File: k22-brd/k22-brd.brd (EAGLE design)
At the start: 22.9 x 63.5 mm, 34 parts, among them J1 61302011121, J2 61302011121, J3 CORTEX_DEBUG_PTH

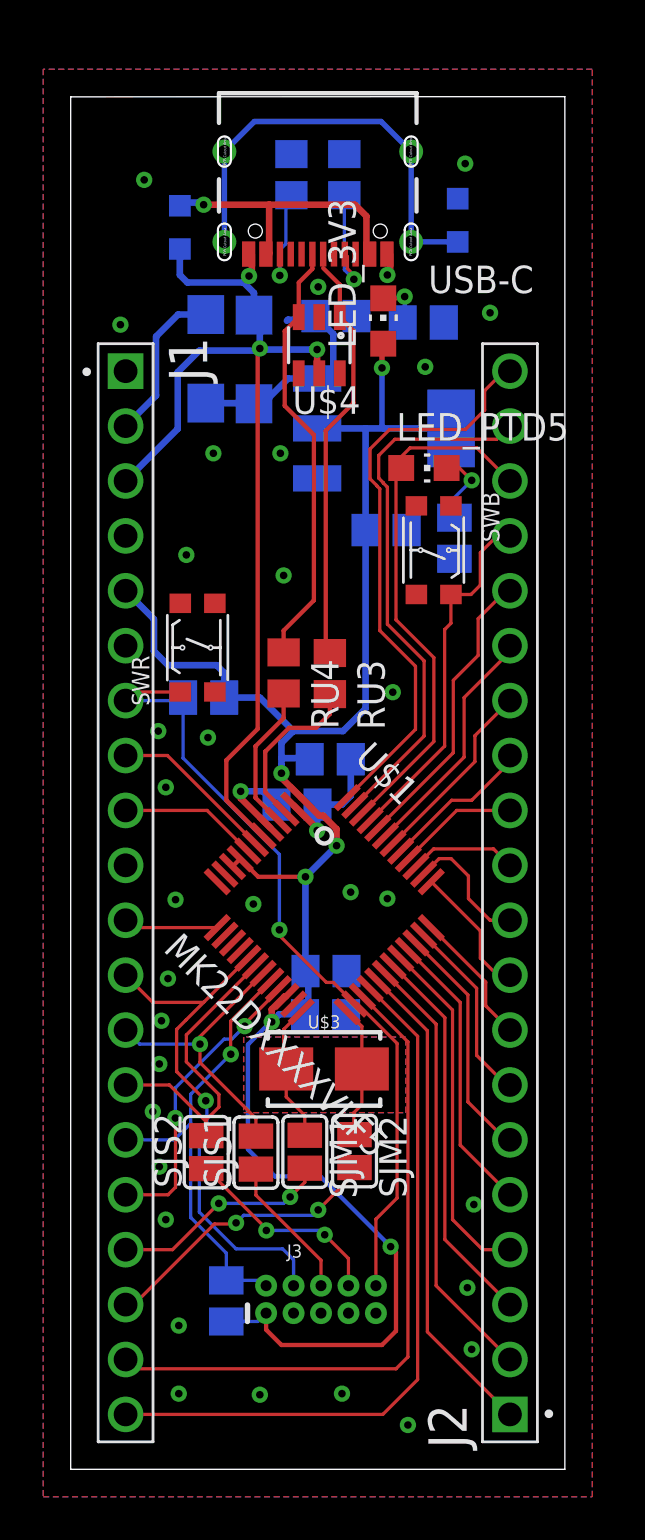
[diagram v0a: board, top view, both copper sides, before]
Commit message: Different pin order on headers
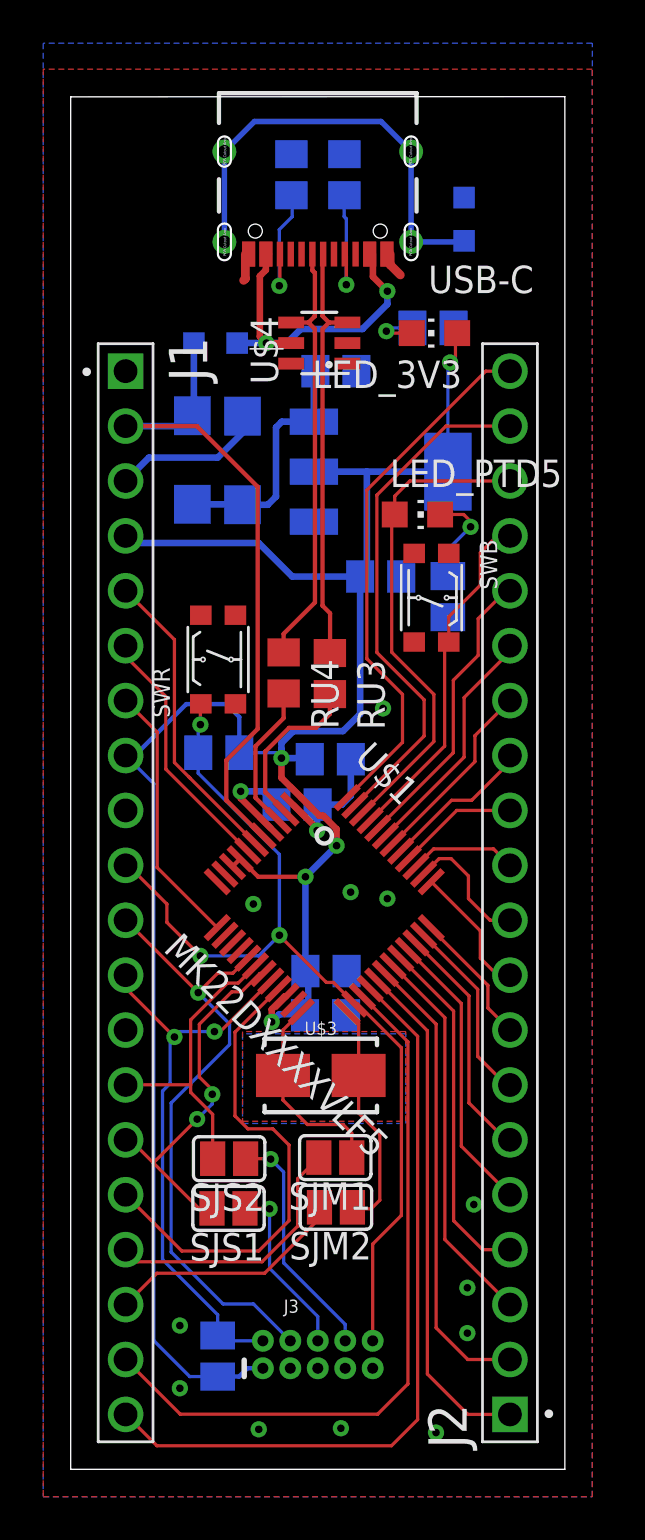
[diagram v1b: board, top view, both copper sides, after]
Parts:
- moved LU1 5.60 mm to (6.70, 52.1), turned to 180 degrees
- moved DV1 5.45 mm to (5.63, 46.7)
- moved DV2 5.00 mm to (7.95, 46.7)
- moved SJS1 2.88 mm to (7.30, 12.1), turned to 180 degrees
- moved SJM2 2.74 mm to (12.3, 12.1), turned to 180 degrees
- moved RL1 2.72 mm to (17.4, 40.4)
- moved RR1 2.64 mm to (6.85, 33.1)
- moved RS2 2.58 mm to (6.80, 5.24)
- moved J3 2.55 mm to (11.4, 5.31)
- moved CV1 2.55 mm to (12.3, 50.8)
- moved LED_3V3 2.44 mm to (16.8, 52.6), turned to 90 degrees
- moved SWB 2.20 mm to (16.7, 40.3)
- moved LED_PTD5 2.17 mm to (16.0, 44.2)
- moved CV2 2.16 mm to (14.3, 41.3)
- moved U$2 2.01 mm to (14.3, 46.1)
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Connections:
- removed net N$5: J1.4
- net 3V3: now also J1.4, J1.8; no longer J1.5
- net D+CON: now also U$4.3; no longer U$4.1
- net D-CON: now also U$4.4; no longer U$4.3
- net DM0: now also J1.6; no longer J1.9
- net DP0: now also J1.5; no longer J1.8
- net GND: now also J1.13, J1.9; no longer J1.10, J1.6
- net RESET: now also J1.10; no longer J1.7
- net SWD_CLK: now also J1.11; no longer J1.12
- net SWD_DIO: now also J1.12; no longer J1.15
- net UART_TX: now also J1.15; no longer J1.13
- net USB5V: now also J1.2; no longer J1.3, U$4.5
- net VBUSCON: now also U$4.5
- net VIN: now also J1.3; no longer J1.2
- net VREF: now also J1.7; no longer J1.11
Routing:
- net 3V3: track 91.7 -> 107.0 mm, vias 6 -> 5
- net USB5V: track 45.7 -> 31.7 mm, vias 2 -> 0
- net PTA4: track 13.8 -> 22.6 mm, vias 2 -> 0
- net VREF: track 4.38 -> 12.3 mm
- net RESET: track 37.4 -> 44.1 mm, vias 1 -> 3
- net DP0: track 7.69 -> 14.2 mm
- net DM0: track 6.44 -> 11.8 mm
- net SWD_DIO: track 21.3 -> 26.7 mm, vias 1 -> 2
- net PTA19_OSC: track 6.14 -> 10.8 mm
- net SWD_CLK: track 24.4 -> 28.6 mm
- net UART_TX: track 13.5 -> 17.0 mm, vias 1 -> 2
- net VBUSCON: track 13.1 -> 16.2 mm, vias 1 -> 2
- net PTA18_OSC: track 6.46 -> 9.39 mm
- net PTB0: track 31.0 -> 33.5 mm
- net PTB1: track 33.2 -> 35.5 mm
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
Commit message: Fixed DRC errors
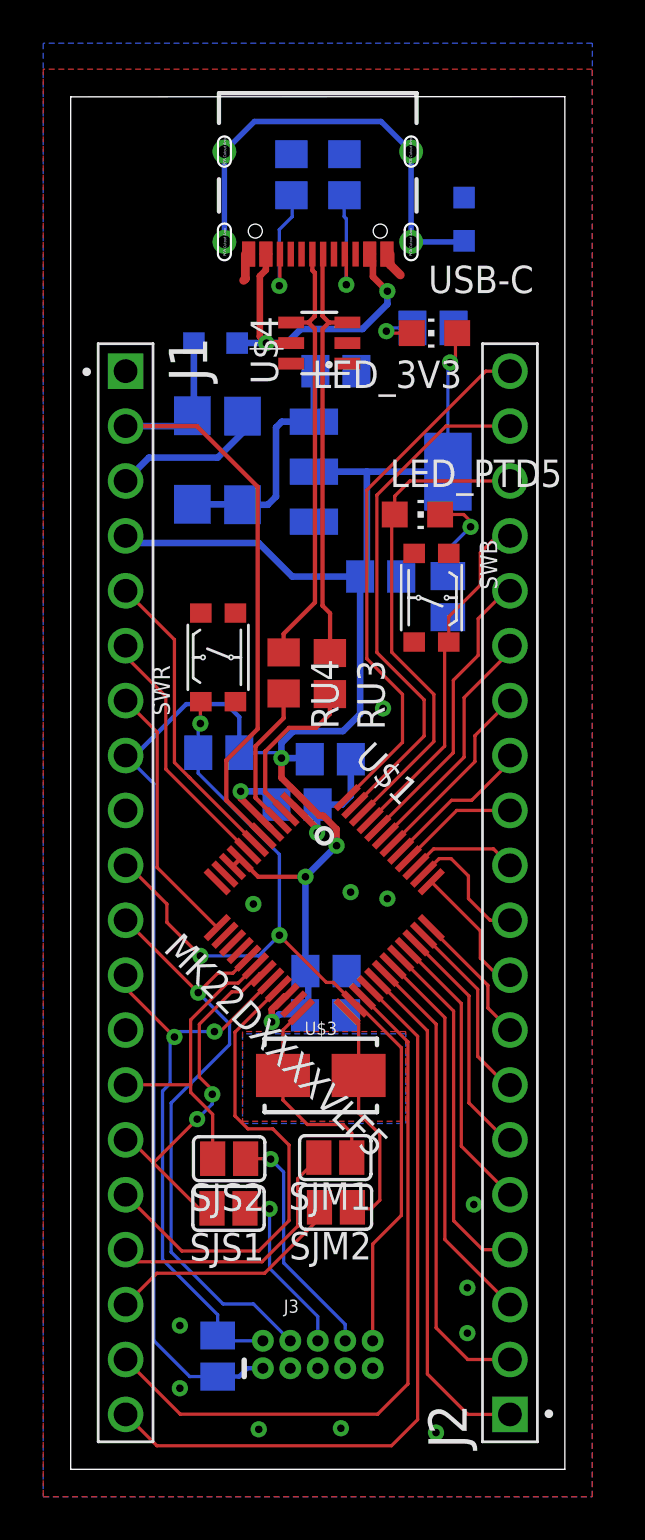
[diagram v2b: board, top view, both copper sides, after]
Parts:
- moved SWR 0.10 mm to (6.82, 37.6)
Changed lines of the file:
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@@
 <attribute name="VALUE" x="13.94" y="43.09" size="0.8128" layer="27" rot="R270"/>
 </element>
-<element name="SWR" library="Switch" library_urn="urn:adsk.eagle:library:11396471" package="KMR731NGLFS" package3d_urn="urn:adsk.eagle:package:17224188/5" value="KMR731NGLFS" x="6.82" y="37.46" smashed="yes" rot="R90">
-<attribute name="CREATED_BY" value="PCBLayout.com" x="50" y="84.45" size="1.778" layer="27" rot="R90" display="off"/>
-<attribute name="DIGIKEY_PARTNO" value="CKN10687CT-ND" x="50" y="84.45" size="1.778" layer="27" rot="R90" display="off"/>
-<attribute name="MANUFACTURER" value="C&amp;K" x="50" y="84.45" size="1.778" layer="27" rot="R90" display="off"/>
-<attribute name="MPN" value="KMR731NG LFS" x="50" y="84.45" size="1.778" layer="27" rot="R90" display="off"/>
-<attribute name="NAME" x="4.59" y="34.77" size="0.8128" layer="25" rot="R90"/>
-<attribute name="VALUE" x="9.57" y="34.69" size="0.8128" layer="27" rot="R90"/>
+<element name="SWR" library="Switch" library_urn="urn:adsk.eagle:library:11396471" package="KMR731NGLFS" package3d_urn="urn:adsk.eagle:package:17224188/5" value="KMR731NGLFS" x="6.82" y="37.56" smashed="yes" rot="R90">
+<attribute name="CREATED_BY" value="PCBLayout.com" x="50" y="84.55" size="1.778" layer="27" rot="R90" display="off"/>
+<attribute name="DIGIKEY_PARTNO" value="CKN10687CT-ND" x="50" y="84.55" size="1.778" layer="27" rot="R90" display="off"/>
+<attribute name="MANUFACTURER" value="C&amp;K" x="50" y="84.55" size="1.778" layer="27" rot="R90" display="off"/>
+<attribute name="MPN" value="KMR731NG LFS" x="50" y="84.55" size="1.778" layer="27" rot="R90" display="off"/>
+<attribute name="NAME" x="4.59" y="34.87" size="0.8128" layer="25" rot="R90"/>
+<attribute name="VALUE" x="9.57" y="34.79" size="0.8128" layer="27" rot="R90"/>
 </element>
 <element name="U$1" library="poli-MK22" package="TQFP48_7X7" value="MK22DXXXXVLF5" x="11.73" y="26.12" smashed="yes" rot="R315">
@@
 <contactref element="U$2" pad="1"/>
 <wire x1="10.315784375" y1="30.71619375" x2="11.4" y2="29.631978125" width="0.3048" layer="1"/>
-<wire x1="11.4" y1="29.631978125" x2="11.4" y2="29.55" width="0.3048" layer="1"/>
-<via x="11.4" y="29.55" extent="1-16" drill="0.35"/>
-<wire x1="11.4" y1="29.55" x2="11.4" y2="30.73" width="0.3048" layer="16"/>
+<wire x1="11.4" y1="29.631978125" x2="11.4" y2="29.45" width="0.3048" layer="1"/>
+<via x="11.4" y="29.45" extent="1-16" drill="0.35"/>
+<wire x1="11.4" y1="29.45" x2="11.4" y2="30.73" width="0.3048" layer="16"/>
 <wire x1="11.4" y1="30.73" x2="11.42" y2="30.75" width="0.3048" layer="16"/>
 <wire x1="11.42" y1="30.75" x2="12.55" y2="30.75" width="0.3048" layer="16"/>
@@
 <wire x1="9.05" y1="52.1" x2="7.7" y2="52.1" width="0.3048" layer="16"/>
 <wire x1="9.05" y1="52.1" x2="10.2" y2="52.1" width="0.3048" layer="1"/>
-<wire x1="13.68" y1="56.215" x2="13.93" y2="55.965" width="0.3048" layer="1"/>
 <wire x1="13.5" y1="52.75" x2="10.65" y2="52.75" width="0.3048" layer="16"/>
 <wire x1="10.65" y1="52.75" x2="10" y2="52.1" width="0.3048" layer="16"/>
@@
 <wire x1="8.75" y1="55.2" x2="8.75" y2="52.4" width="0.3048" layer="1"/>
 <wire x1="8.75" y1="52.4" x2="9.05" y2="52.1" width="0.3048" layer="1"/>
-<wire x1="13.98" y1="56.215" x2="13.98" y2="55.17" width="0.3048" layer="1"/>
 <wire x1="13.98" y1="55.17" x2="14.65" y2="54.5" width="0.3048" layer="1"/>
 <via x="14.65" y="54.5" extent="1-16" drill="0.35"/>
 <wire x1="14.65" y1="54.5" x2="14.65" y2="53.9" width="0.3048" layer="16"/>
 <wire x1="14.65" y1="53.9" x2="13.5" y2="52.75" width="0.3048" layer="16"/>
-<wire x1="13.98" y1="56.215" x2="13.93" y2="55.965" width="0" layer="19" extent="1-1"/>
-<wire x1="8.88" y1="56.215" x2="9.18" y2="56.215" width="0" layer="19" extent="1-1"/>
+<wire x1="13.68" y1="56.215" x2="13.98" y2="55.915" width="0.3048" layer="1"/>
+<wire x1="13.98" y1="55.915" x2="13.98" y2="55.17" width="0.3048" layer="1"/>
+<wire x1="13.98" y1="56.215" x2="13.68" y2="56.215" width="0.3048" layer="1"/>
+<wire x1="9.18" y1="56.215" x2="8.88" y2="56.215" width="0.3048" layer="1"/>
 </signal>
 <signal name="CC1CON">
@@
 <contactref element="U$4" pad="4"/>
 <wire x1="11.3" y1="40.1" x2="9.85" y2="38.65" width="0.2" layer="1"/>
-<wire x1="11.3" y1="52.6" x2="11.3" y2="40.1" width="0.2" layer="1"/>
 <wire x1="11.2968" y1="55.3482" x2="11.18" y2="55.465" width="0.2032" layer="1"/>
 <wire x1="11.18" y1="56.215" x2="11.18" y2="55.465" width="0.2032" layer="1"/>
@@
 <wire x1="11.2968" y1="53.3468" x2="11" y2="53.05" width="0.2032" layer="1"/>
 <wire x1="11" y1="53.05" x2="10.2" y2="53.05" width="0.2032" layer="1"/>
-<wire x1="11.2968" y1="52.7532" x2="11.2968" y2="52.60369375" width="0.2032" layer="1"/>
-<wire x1="11.2968" y1="52.60369375" x2="11.2984" y2="52.60209375" width="0.2032" layer="1"/>
-<wire x1="11.2984" y1="52.60209375" x2="11.2984" y2="52.6" width="0.2032" layer="1"/>
 <wire x1="11" y1="53.05" x2="11.2968" y2="52.7532" width="0.2032" layer="1"/>
+<wire x1="11.2968" y1="52.7532" x2="11.2984" y2="52.7516" width="0.2" layer="1"/>
+<wire x1="11.2984" y1="52.7516" x2="11.2984" y2="52.6043625" width="0.2" layer="1"/>
+<wire x1="11.2984" y1="52.6043625" x2="11.3" y2="52.6027625" width="0.2" layer="1"/>
+<wire x1="11.3" y1="52.6027625" x2="11.3" y2="40.1" width="0.2" layer="1"/>
 <wire x1="11.18" y1="56.215" x2="12.18" y2="56.215" width="0" layer="19" extent="1-1"/>
-<wire x1="11.3" y1="52.6" x2="11.2984" y2="52.6" width="0" layer="19" extent="1-1"/>
 </signal>
 <signal name="CC2CON">
@@
 <wire x1="5.63" y1="48.53" x2="5.63" y2="48.74" width="0.3048" layer="16"/>
 <wire x1="5.36" y1="48.26" x2="5.63" y2="48.53" width="0.3048" layer="16"/>
-<wire x1="5.55" y1="48.82" x2="5.63" y2="48.74" width="0.3048" layer="16"/>
 <wire x1="8.65" y1="34.25" x2="8.65" y2="45.45" width="0.2032" layer="1"/>
 <wire x1="5.84" y1="48.26" x2="2.54" y2="48.26" width="0.2032" layer="1"/>
@@
 <contactref element="RU3" pad="2"/>
 <contactref element="U$1" pad="3"/>
-<wire x1="11.99" y1="35.86" x2="11.89" y2="35.76" width="0.2" layer="1"/>
 <wire x1="10.1" y1="34.3" x2="9" y2="33.2" width="0.2" layer="1"/>
 <wire x1="9" y1="31.324871875" x2="9.96223125" y2="30.362640625" width="0.2" layer="1"/>
@@
 <contactref element="J3" pad="2"/>
 <contactref element="RS2" pad="2"/>
-<wire x1="6.8" y1="6.19" x2="6.75" y2="6.24" width="0.1524" layer="16"/>
 <wire x1="8.89" y1="5.945" x2="7.045" y2="5.945" width="0.1524" layer="16"/>
 <wire x1="7.045" y1="5.945" x2="6.8" y2="6.19" width="0.1524" layer="16"/>
@@
 <contactref element="U$1" pad="21"/>
 <contactref element="J1" pad="16"/>
-<wire x1="9.608678125" y1="22.2309125" x2="9.608678125" y2="22.158678125" width="0.1524" layer="1"/>
 <wire x1="9.608678125" y1="22.2309125" x2="7.6" y2="20.222234375" width="0.1524" layer="1"/>
 <wire x1="7.6" y1="20.222234375" x2="7.6" y2="16.35" width="0.1524" layer="1"/>
@@
 <wire x1="9.655190625" y1="24.694809375" x2="11.826196875" y2="22.523803125" width="0.1524" layer="1"/>
 <contactref element="J1" pad="10"/>
-<wire x1="5.9" y1="33.15" x2="5.9" y2="34.35" width="0.1524" layer="16"/>
-<wire x1="5.9" y1="34.35" x2="6" y2="34.45" width="0.1524" layer="16"/>
-<via x="6" y="34.45" extent="1-16" drill="0.35"/>
-<wire x1="6" y1="34.45" x2="6" y2="35.39" width="0.1524" layer="1"/>
-<wire x1="6" y1="35.39" x2="6.02" y2="35.41" width="0.1524" layer="1"/>
-<wire x1="9.655190625" y1="24.705190625" x2="9.555190625" y2="24.605190625" width="0.1524" layer="16"/>
+<wire x1="5.9" y1="33.15" x2="5.9" y2="34.4" width="0.1524" layer="16"/>
+<wire x1="5.9" y1="34.4" x2="6" y2="34.5" width="0.1524" layer="16"/>
+<via x="6" y="34.5" extent="1-16" drill="0.35"/>
+<wire x1="6" y1="34.5" x2="6" y2="35.49" width="0.1524" layer="1"/>
+<wire x1="6" y1="35.49" x2="6.02" y2="35.51" width="0.1524" layer="1"/>
 <wire x1="9.655190625" y1="24.705190625" x2="8.7" y2="23.75" width="0.1524" layer="16"/>
 <wire x1="8.7" y1="23.75" x2="6" y2="23.75" width="0.1524" layer="16"/>
@@
 <wire x1="9.3" y1="20.7" x2="9.3" y2="21.27905" width="0.3048" layer="1"/>
 <wire x1="9.89830625" y1="21.87735625" x2="9.96223125" y2="21.87735625" width="0.3048" layer="1"/>
-<wire x1="9.75" y1="33.3" x2="9.75" y2="32.9" width="0.3048" layer="16"/>
 <wire x1="11.06" y1="32.85" x2="11.01" y2="32.9" width="0.3048" layer="16"/>
 <via x="9.75" y="32.9" extent="1-16" drill="0.35"/>
@@
 <wire x1="8.67223125" y1="27.41" x2="10.86" y2="27.41" width="0.2" layer="1"/>
 <via x="10.86" y="27.41" extent="1-16" drill="0.35"/>
-<wire x1="9.3" y1="20.7" x2="9.25" y2="20.7" width="0.2" layer="16"/>
 <wire x1="11.2512" y1="46.15" x2="13.7" y2="46.15" width="0.3048" layer="16"/>
 <wire x1="13.7" y1="46.15" x2="17.449" y2="46.15" width="0.3048" layer="16"/>
@@
 <wire x1="5.63" y1="44.64" x2="7.93" y2="44.64" width="0.3048" layer="16"/>
 <wire x1="7.93" y1="44.64" x2="7.95" y2="44.62" width="0.3048" layer="16"/>
-<wire x1="11.2012" y1="48.5114" x2="11.2512" y2="48.4614" width="0.3048" layer="16"/>
 <wire x1="11.32" y1="50.8" x2="11.2512" y2="50.7312" width="0.3048" layer="16"/>
 <wire x1="11.2512" y1="50.7312" x2="11.2512" y2="48.4614" width="0.3048" layer="16"/>
@@
 <wire x1="9.5" y1="45" x2="9.5" y2="48.2" width="0.3048" layer="16"/>
 <wire x1="9.5" y1="48.2" x2="9.7614" y2="48.4614" width="0.3048" layer="16"/>
+<wire x1="9.12" y1="44.62" x2="9.5" y2="45" width="0.3048" layer="16"/>
 <wire x1="9.7614" y1="48.4614" x2="11.2512" y2="48.4614" width="0.3048" layer="16"/>
-<wire x1="9.12" y1="44.62" x2="9.5" y2="45" width="0.3048" layer="16"/>
 </signal>
 <signal name="VIN">
